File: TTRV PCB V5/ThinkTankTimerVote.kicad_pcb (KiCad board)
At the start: 2 copper layers, 32 x 79.7 mm, 22 parts, among them J1 BattLeft, J2 Conn_01x02, J4 Conn_01x04, Q1 IRLML2060, SW1 SW_DPDT_x2, SW2 SW_Push, SW3 SW_Push, SW4 SW_Push, U2 HT75xx-1-SOT89, U3 LTC4054ES5-4.2

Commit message: Update PCB
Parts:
- C1, C2, C3: footprint Capacitor_SMD:C_0402_1005Metric -> Capacitor_SMD:C_0603_1608Metric
- D1: footprint LED_SMD:LED_0603_1608Metric -> LED_SMD:LED_0805_2012Metric
- R1, R2, R3, R4: footprint Resistor_SMD:R_0402_1005Metric -> Resistor_SMD:R_0603_1608Metric
- moved C2 2.08 mm to (194.9, 119.4)
- moved D1 1.82 mm to (172.1, 71.7)
- moved C1 1.18 mm to (198.7, 119.3)
- moved R2 0.38 mm to (196.8, 123.4)
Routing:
- net GND: track 166.2 -> 0.00 mm
- net +3V3: track 114.4 -> 0.00 mm, vias 1 -> 0
- net Batt+: track 108.1 -> 0.00 mm, vias 1 -> 0
- net VILDO: track 59.6 -> 0.00 mm, vias 1 -> 0
- net +5V: track 58.4 -> 0.00 mm
- net Right: track 48.8 -> 0.00 mm
- net MotSig: track 45.9 -> 0.00 mm
- net Middle: track 39.6 -> 0.00 mm
- net Left: track 36.1 -> 0.00 mm
- net Motor-: track 24.8 -> 0.00 mm
- net SDA: track 18.5 -> 0.00 mm
- net SCL: track 17.0 -> 0.00 mm
- net Net-(U3-PROG): track 10.3 -> 0.00 mm
- net Net-(Q1-G): track 8.35 -> 0.00 mm
- net Net-(U3-V_{CC}): track 4.75 -> 0.00 mm
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
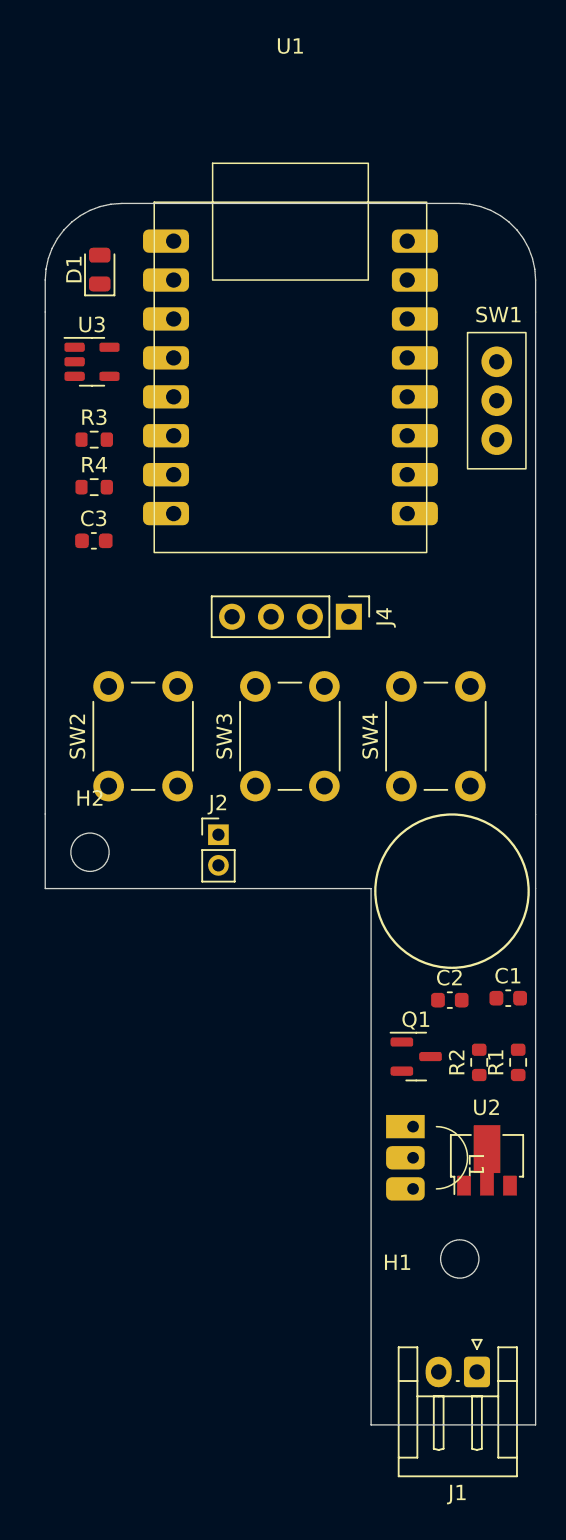
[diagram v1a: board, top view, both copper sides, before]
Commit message: PCB Update
Includes Artwork and Rough Draft KiCad Files
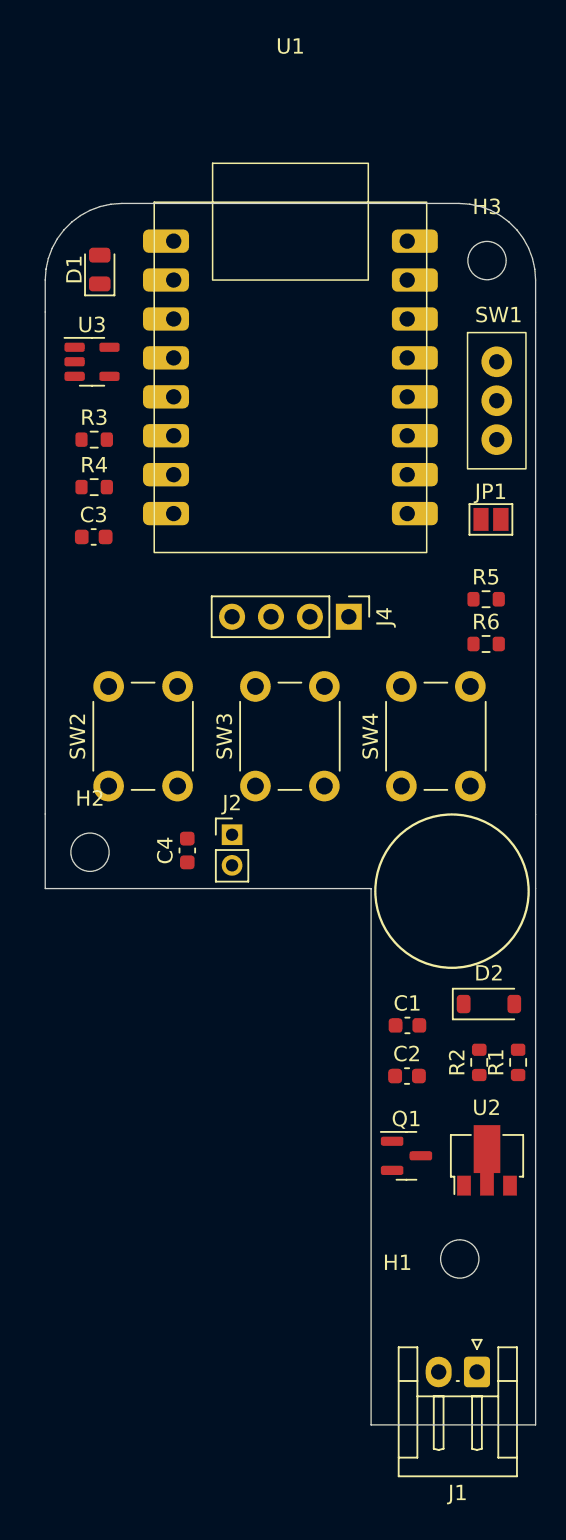
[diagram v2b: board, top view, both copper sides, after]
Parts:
- removed L1: MCP1700x-120xxMB, OpenMuscleDevKit:LDO33
- added C4: 100 uF, Capacitor_SMD:C_0603_1608Metric, F.Cu at (177.8, 109.6)
- added D2: 1N4007, Diode_SMD:D_SOD-123, F.Cu at (197.5, 119.6)
- added H3: MountingHole, MountingHole:MountingHole_2.5mm, F.Cu at (197.4, 71.1)
- added JP1: 5V Jump, Jumper:SolderJumper-2_P1.3mm_Open_Pad1.0x1.5mm, F.Cu at (197.6, 88.0)
- added R5: 10k, Resistor_SMD:R_0603_1608Metric, F.Cu at (197.3, 93.2)
- added R6: 20k, Resistor_SMD:R_0603_1608Metric, F.Cu at (197.3, 96.1)
- R4: value 5.1k -> 2.7k
- moved C1 6.81 mm to (192.2, 121.0)
- moved Q1 6.51 mm to (192.1, 129.5)
- moved C2 5.69 mm to (192.1, 124.3)
- moved J2 0.89 mm to (180.7, 108.6)
- moved C3 0.25 mm to (171.7, 89.2)
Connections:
- J2 pad 1: +3V3 -> Batt+
- SW1 pad 3: +5V -> Net-(JP1-B)
- U1 pad 0: unconnected-(U1-GPIO0-Pad0) -> MotSig
- U1 pad 1: unconnected-(U1-GPIO1-Pad1) -> ADC1_BAT
- U1 pad 20: ScreenSig -> unconnected-(U1-GPIO20-Pad20)
- U1 pad 21: MotSig -> unconnected-(U1-GPIO21-Pad21)

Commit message: PCB V 2.6.0
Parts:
- added J3: Conn_02x03_Odd_Even, Connector_PinHeader_2.54mm:PinHeader_2x03_P2.54mm_Vertical, F.Cu at (170.9, 95.0)
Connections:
- U1 pad 10: unconnected-(U1-GPIO10-Pad10) -> GPIO10
- U1 pad 20: unconnected-(U1-GPIO20-Pad20) -> GPIO20
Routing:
- net GND: track 0.00 -> 174.9 mm
- net Batt+: track 0.00 -> 133.8 mm, vias 0 -> 1
- net +3V3: track 0.00 -> 88.9 mm
- net VILDO: track 0.00 -> 75.2 mm, vias 0 -> 2
- net +5V: track 0.00 -> 62.2 mm
- net Motor-: track 0.00 -> 54.1 mm, vias 0 -> 1
- net Right: track 0.00 -> 48.8 mm
- net MotSig: track 0.00 -> 40.6 mm
- net Middle: track 0.00 -> 39.6 mm
- net Left: track 0.00 -> 39.0 mm
- net ADC2: track 0.00 -> 24.0 mm
- net ADC3: track 0.00 -> 21.3 mm
- net SCL: track 0.00 -> 20.7 mm
- net SDA: track 0.00 -> 18.5 mm
- net GPIO10: track 0.00 -> 14.5 mm
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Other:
- board text added: "+ -"
